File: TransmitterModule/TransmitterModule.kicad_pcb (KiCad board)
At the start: 2 copper layers, 94.6 x 45.6 mm, 22 parts, among them J3 Battery, U1 NRF24L01_, U3 102010388, U4 LD1086DTTR

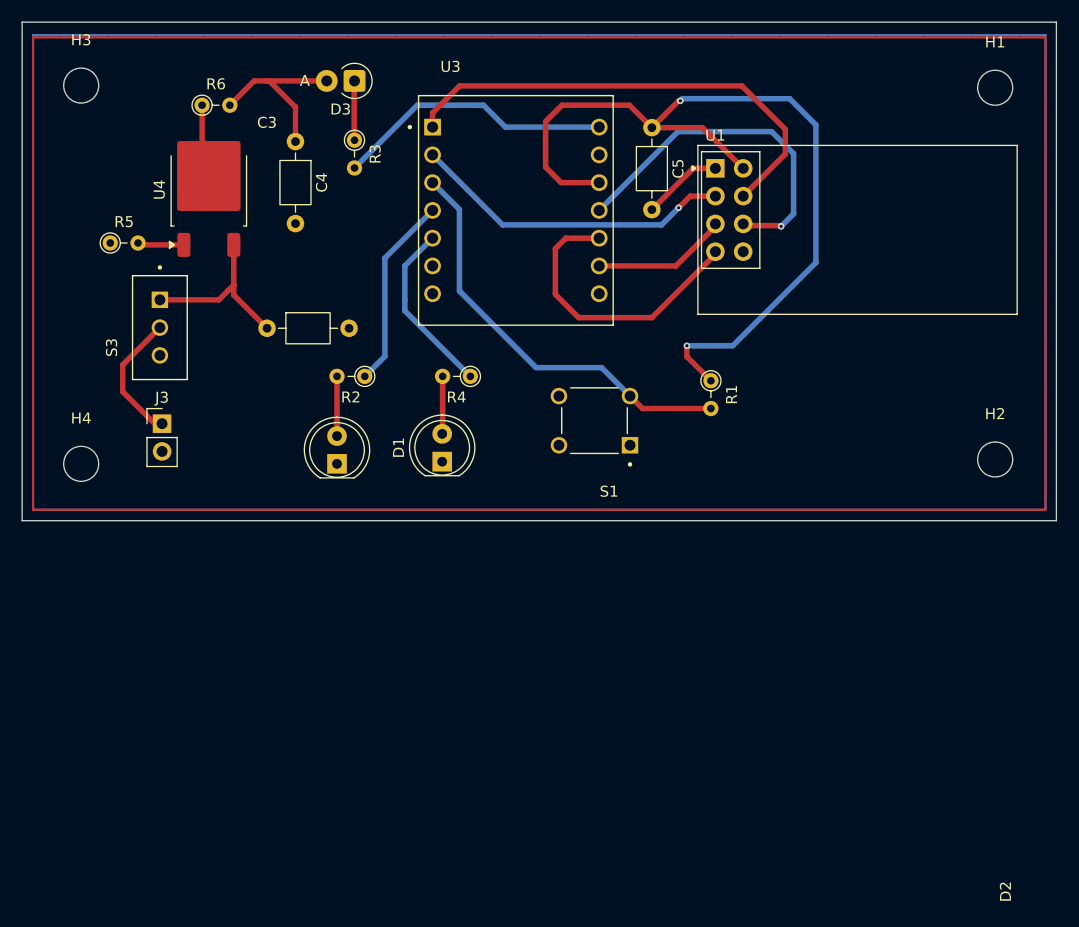
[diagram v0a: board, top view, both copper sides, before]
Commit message: updated transmitter module to delete LOD and change button layout
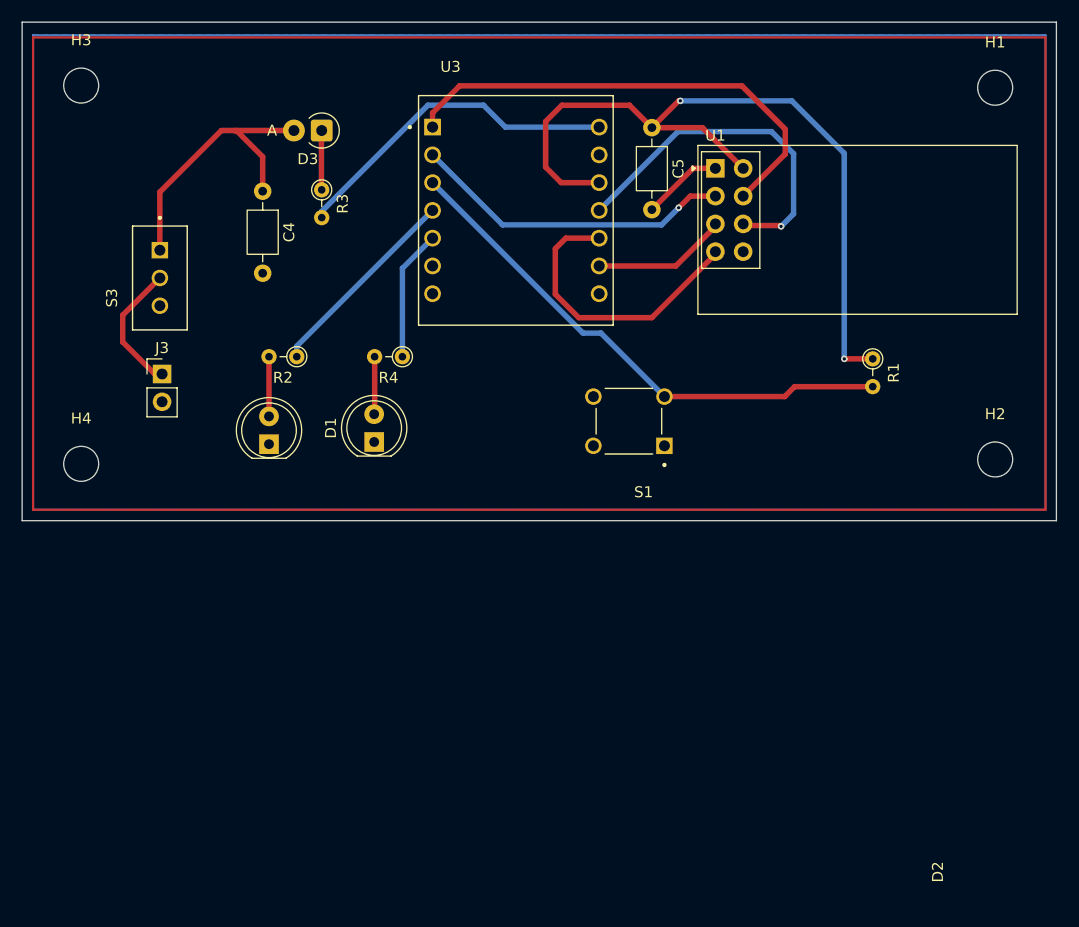
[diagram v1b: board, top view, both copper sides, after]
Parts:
- removed C3: 10u, Capacitor_THT:C_Axial_L3.8mm_D2.6mm_P7.50mm_Horizontal
- removed R5: 360, Resistor_THT:R_Axial_DIN0204_L3.6mm_D1.6mm_P2.54mm_Vertical
- removed R6: 120, Resistor_THT:R_Axial_DIN0204_L3.6mm_D1.6mm_P2.54mm_Vertical
- removed U4: LD1086DTTR, Package_TO_SOT_SMD:TO-252-2
- moved R1 14.9 mm to (191.4, 132.4)
- moved D1 6.48 mm to (145.8, 140.0)
- moved D2 6.48 mm to (136.2, 140.2)
- moved R2 6.48 mm to (138.7, 132.2)
- moved R4 6.48 mm to (148.4, 132.2)
- moved C4 5.44 mm to (135.6, 117.1)
- moved D3 5.44 mm to (141.0, 111.5)
- moved R3 5.44 mm to (141.0, 116.9)
- moved J3 4.54 mm to (126.4, 133.8)
- moved S3 4.54 mm to (126.2, 125.0)
- moved S1 3.15 mm to (169.1, 138.1)
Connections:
- C4 pad 1: Net-(D3-A) -> /Regulator_In
- D3 pad 2: Net-(D3-A) -> /Regulator_In
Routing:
- net Net-(D3-A): track 16.5 -> 0.00 mm
- net /DIG_IN: track 38.4 -> 48.7 mm
- net /Regulator_In: track 16.6 -> 26.6 mm
- net /VCC: track 79.5 -> 72.7 mm
- net Net-(U4-OUT): track 6.73 -> 0.00 mm
- net /5V_IN: track 25.6 -> 30.8 mm
- net Net-(U4-ADJ/GND): track 4.27 -> 0.00 mm
- net /LED_ON2: track 16.2 -> 12.0 mm
- net /LED_ON1: track 17.7 -> 18.5 mm

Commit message: added net id and name
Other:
- board text added: "ag821 Alisha Gupta"
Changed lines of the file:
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@@
 		(layer "Edge.Cuts")
+	)
+	(gr_text "ag821 Alisha Gupta"
+		(at 175.4 143.6 0)
+		(layer "F.Cu")
+		(effects
+			(font
+				(size 1.5 1.5)
+				(thickness 0.3)
+				(bold yes)
+			)
+			(justify left bottom)
+		)
 	)
 	(segment
